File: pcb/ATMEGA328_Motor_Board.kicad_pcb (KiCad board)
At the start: 2 copper layers, 77 x 100 mm, 145 parts, among them P1 CONN_01X04, P10 CONN_01X04, P11 CONN_01X02, P12 CONN_01X03, P13 CONN_01X02, P14 USB_MINI, P15 CONN_01X02, P16 CONN_02X03, P2 CONN_01X04, P3 CONN_01X03, P4 CONN_01X03, P5 CONN_01X03, P6 CONN_01X03, P7 CONN_01X03, P8 CONN_01X03, P9 CONN_01X04, SW1 Pulsador_4p, U1 ATMEGA328, U2 PCA9685, U3 FT231X, U4 L298P, U5 L298P, U6 TSR_1, U7 LM2903, U8 LM2903

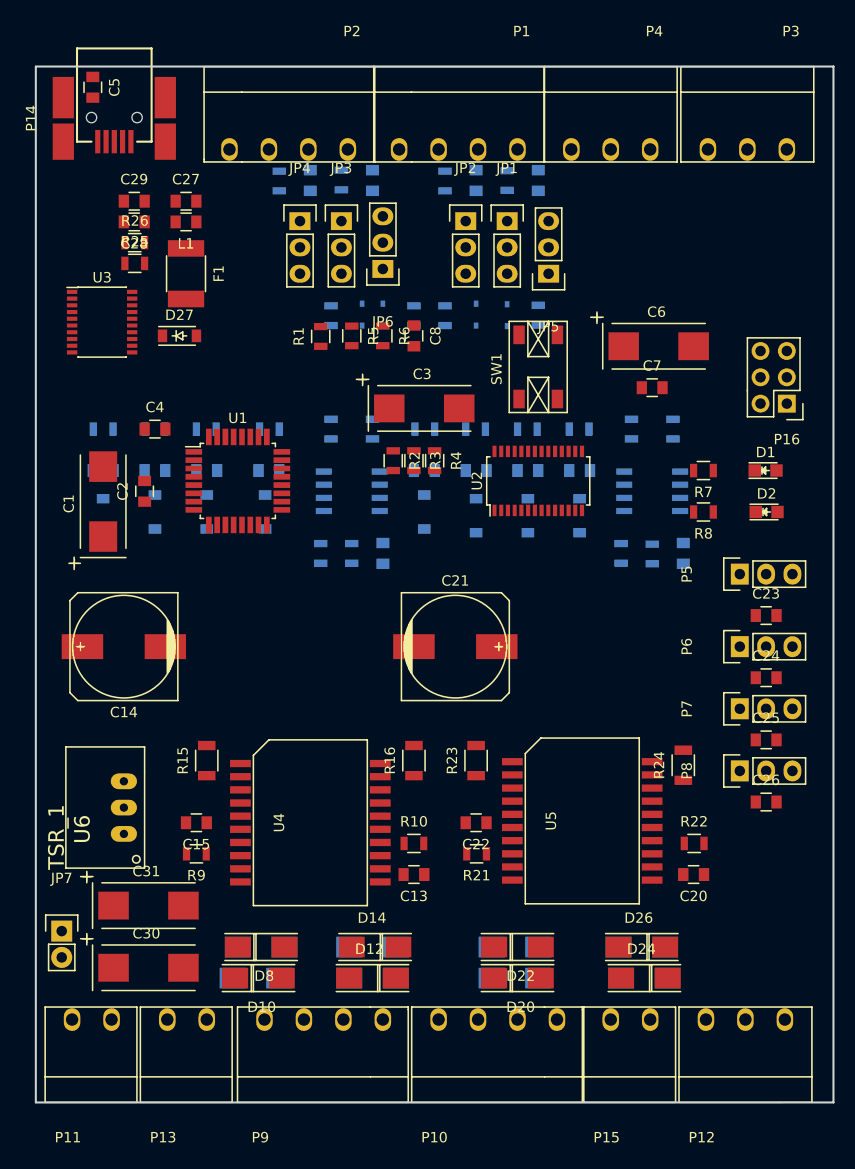
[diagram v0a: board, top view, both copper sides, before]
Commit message: añadida huella para choke alimentacion
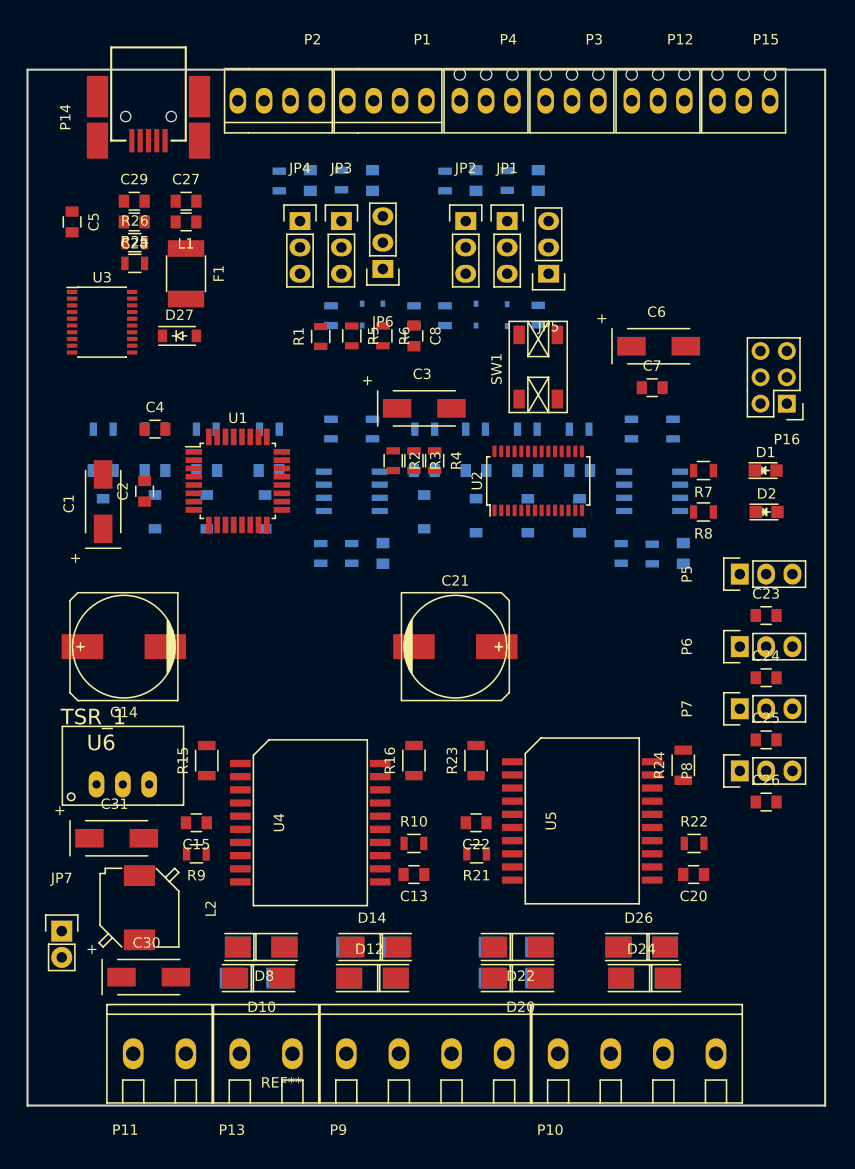
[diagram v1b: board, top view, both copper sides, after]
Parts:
- added L2: 10u, Magneticos:FERROCORE_SMD_0703, F.Cu at (118.5, 121.2)
- C1, C3, C30, C31, C6: footprint Condensadores:TantalC_SizeD_EIA-7343_Wave -> Condensadores:TantalC_SizeC_EIA-6032_Wave
- P1, P2: footprint PhoenixContact:PhoenixContact_MC_1_5x4x3_81 -> PhoenixContact:PhoenixContact_MPT_0,5_4-2,54
- P10, P9: footprint PhoenixContact:PhoenixContact_MC_1_5x4x3_81 -> PhoenixContact:PhoenixContact_mkdsn_4_5.08
- P11, P13: footprint PhoenixContact:PhoenixContact_MC_1_5x2x3_81 -> PhoenixContact:PhoenixContact_mkdsn_2_5.08
- P12, P3, P4: footprint PhoenixContact:PhoenixContact_MC_1_5x3x3_81 -> PhoenixContact:PhoenixContact_MPT_0,5_3-2,54
- P15: footprint PhoenixContact:PhoenixContact_MC_1_5x2x3_81 -> PhoenixContact:PhoenixContact_MPT_0,5_3-2,54
- REF**: moved to F.Cu
- moved P15 90.0 mm to (179.4, 43.3), turned to 180 degrees
- moved P12 88.7 mm to (171.1, 43.3), turned to 180 degrees
- moved P3 18.8 mm to (162.8, 43.3)
- moved P4 14.1 mm to (154.5, 43.3)
- moved C5 13.2 mm to (112.0, 55.0)
- moved P10 12.0 mm to (158.9, 135.3)
- moved U6 10.0 mm to (111.1, 111.3), turned to 0 degrees
- moved P1 9.98 mm to (146.2, 43.3)
- moved P9 8.56 mm to (138.5, 135.3)
- moved P13 7.74 mm to (128.2, 135.3)
- moved C31 7.19 mm to (116.3, 114.5)
- moved P11 6.76 mm to (117.9, 135.3)
- moved P2 5.58 mm to (135.6, 43.3)
- moved P14 3.30 mm to (119.4, 47.1)
- moved C30 0.90 mm to (119.4, 127.9)
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
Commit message: se añaden optos para E/S y cristal
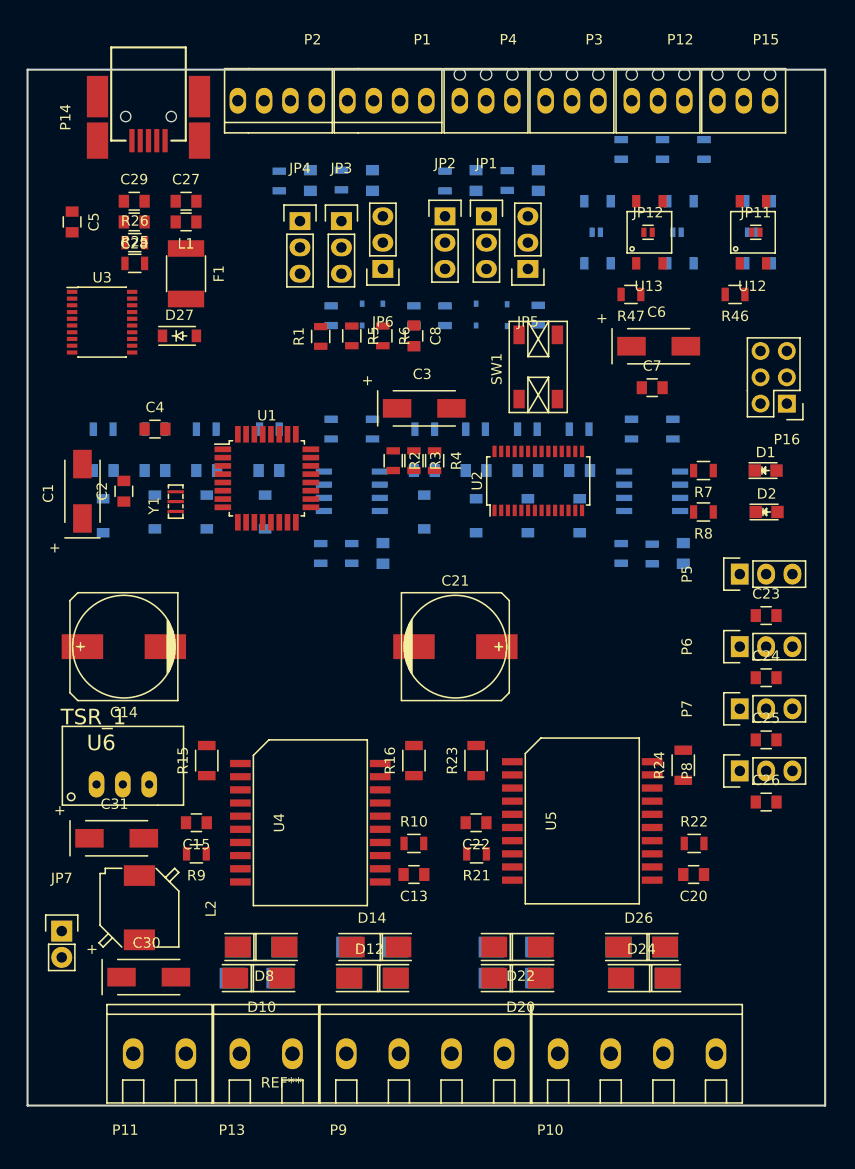
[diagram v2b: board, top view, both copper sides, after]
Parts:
- added JP10: Jumper_NO_Small, Vias:JMP_0603, B.Cu at (177.6, 56.0)
- added JP11: Jumper_NO_Small, Vias:JMP_0603, F.Cu at (178.0, 56.0)
- added JP12: Jumper_NO_Small, Vias:JMP_0603, F.Cu at (167.6, 56.0)
- added JP8: Jumper_NO_Small, Vias:JMP_0603, B.Cu at (162.6, 56.0)
- added JP9: Jumper_NO_Small, Vias:JMP_0603, B.Cu at (170.4, 56.0)
- added R43: R, Resistors_SMD:R_0805, B.Cu at (165.0, 48.0)
- added R44: R, Resistors_SMD:R_0805, B.Cu at (169.0, 48.0)
- added R45: R, Resistors_SMD:R_0805, B.Cu at (173.0, 48.0)
- added R46: R, Resistors_SMD:R_0805, F.Cu at (176.0, 62.0)
- added R47: R, Resistors_SMD:R_0805, F.Cu at (165.9, 62.0)
- added U10: VOM617A, SOP:SOP-4, B.Cu at (172.0, 59.0)
- added U11: VOM617A, SOP:SOP-4, B.Cu at (179.5, 59.0)
- added U12: ASSR-1218, SOP:SOP-4, F.Cu at (176.5, 59.0)
- added U13: ASSR-1218, SOP:SOP-4, F.Cu at (166.5, 59.0)
- added U9: VOM617A, SOP:SOP-4, B.Cu at (164.0, 59.0)
- added Y1: 16MHz, Cristal:Murata_CSTCE_V_A, F.Cu at (122.0, 82.0)
- moved U1 2.81 mm to (130.8, 79.8)
- moved C1 2.24 mm to (113.0, 81.0)
- moved JP1 2.05 mm to (152.0, 54.5)
- moved JP2 2.05 mm to (148.0, 54.5)
- moved JP5 2.05 mm to (156.0, 59.5)
- moved C2 2.00 mm to (117.0, 81.0)
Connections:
- U1 pad 10: DI1 -> uC_DI1
- U1 pad 11: DI2 -> uC_DI2
- U1 pad 12: DI3 -> uC_DI3
- U1 pad 13: DO1 -> uC_DO1
- U1 pad 14: DO2 -> uC_DO2

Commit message: comienzo a ordenar paquetes y rutado de potencia
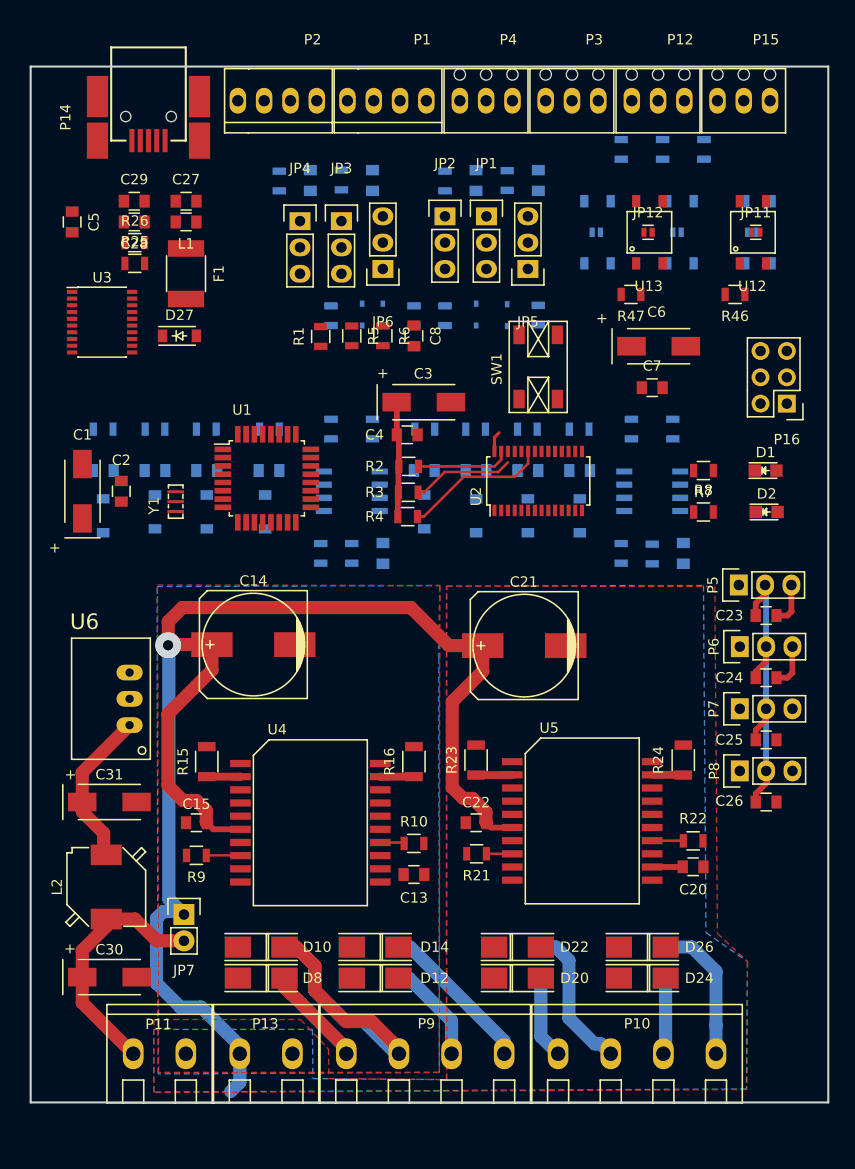
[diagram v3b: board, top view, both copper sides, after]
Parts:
- moved C4 24.4 mm to (144.3, 75.5)
- moved C14 12.5 mm to (129.5, 95.8)
- moved JP7 11.9 mm to (122.8, 121.9)
- moved U6 9.57 mm to (119.5, 106.9), turned to 90 degrees
- moved C21 6.65 mm to (155.7, 95.9), turned to 180 degrees
- moved R4 5.99 mm to (144.4, 83.5), turned to 0 degrees
- moved C30 3.80 mm to (115.6, 127.9)
- moved L2 3.77 mm to (115.3, 119.2)
- moved C31 3.57 mm to (115.6, 111.0)
- moved R3 3.10 mm to (144.4, 81.1), turned to 0 degrees
- moved D10 3.01 mm to (130.2, 125.0), turned to 180 degrees
- moved D11 3.01 mm to (141.2, 128.0), turned to 0 degrees
- moved D13 3.01 mm to (141.2, 125.0), turned to 0 degrees
- moved D19 3.01 mm to (155.0, 128.0)
- moved D21 3.01 mm to (155.0, 125.0)
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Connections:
- C30 pad 1: VSS -> +24V
- L2 pad 1: VSS -> +24V
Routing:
- net VSS: track 0.00 -> 137.9 mm, vias 0 -> 1
- net +5V: track 0.00 -> 47.2 mm
- net Motor1-: track 0.00 -> 33.7 mm
- net +24V: track 0.00 -> 24.4 mm
- net Motor1+: track 0.00 -> 19.6 mm
- net Net-(C31-Pad1): track 0.00 -> 15.4 mm
- net Motor2-: track 0.00 -> 15.2 mm
- net Motor3-: track 0.00 -> 14.3 mm
- net /Control/PWM_OE: track 0.00 -> 14.0 mm
- net Motor4-: track 0.00 -> 13.8 mm
- net Motor2+: track 0.00 -> 10.0 mm
- net /Control/SCL: track 0.00 -> 9.87 mm
- net /Control/SDA: track 0.00 -> 9.05 mm
- net GND: track 0.00 -> 8.43 mm
- net Motor3+: track 0.00 -> 7.99 mm
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- added copper zone on B.Cu, net GND
- added copper zone on F.Cu, net GND
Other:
- net class Default: clearance 0.2 -> 0.2032; trace_width 0.25 -> 0.254
- net class Potencia added: clearance 0.4064, trace_width 1.27, via_dia 4, via_drill 1
- rule trace_clearance: 0.2 -> 0.2032

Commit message: finalizado el posicionado sobre la pcb
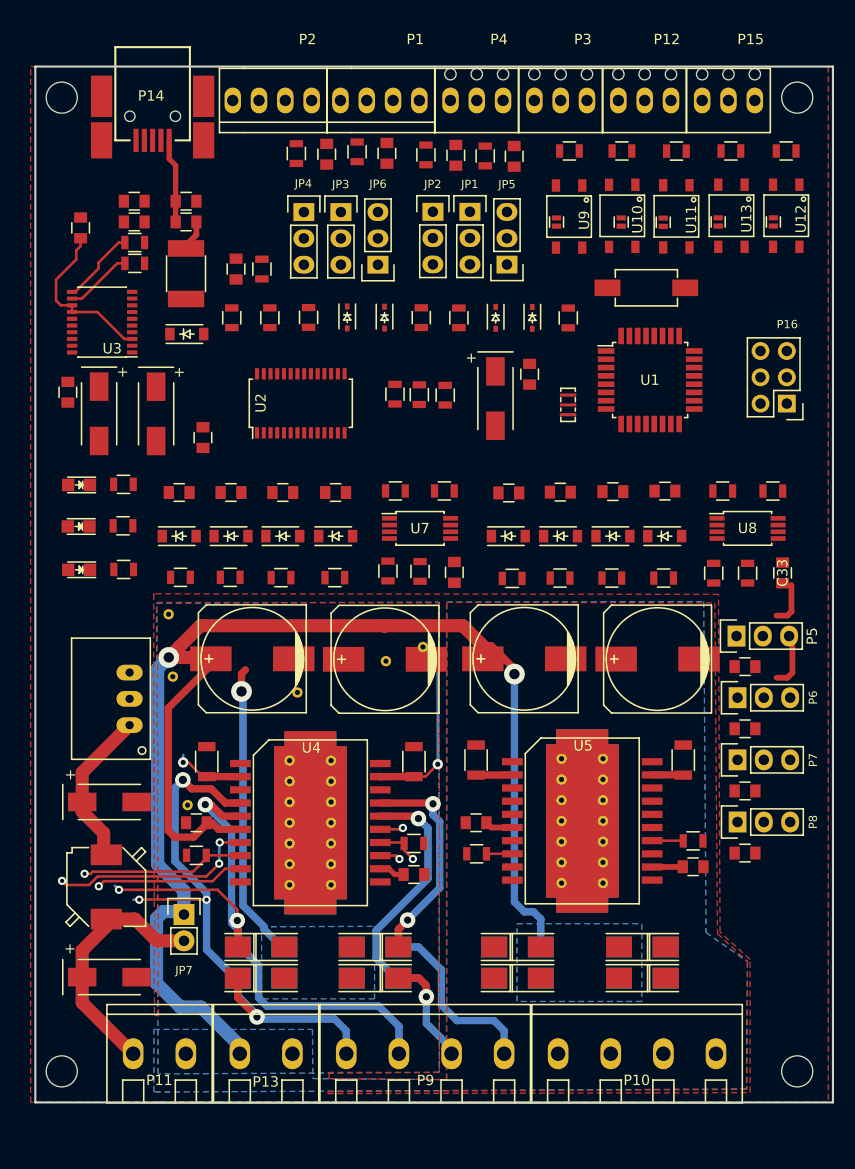
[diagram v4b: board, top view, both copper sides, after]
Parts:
- added C38: 220u, Capacitors_SMD:c_elec_10x10, F.Cu at (142.2, 97.2)
- added C39: 220u, Capacitors_SMD:c_elec_10x10, F.Cu at (168.5, 97.2)
- added D32: LED, Leds:LED_0805, F.Cu at (112.7, 88.6)
- added Gnd-Via: VAL**, Vias:Gnd-Via, F.Cu at (182.0, 137.0)
- added Gnd-Via: VAL**, Vias:Gnd-Via, F.Cu at (145.9, 96.0)
- added Gnd-Via: VAL**, Vias:Gnd-Via, F.Cu at (182.0, 43.0)
- added Gnd-Via: VAL**, Vias:Gnd-Via, F.Cu at (111.0, 43.0)
- added Gnd-Via: VAL**, Vias:Gnd-Via, F.Cu at (111.0, 137.0)
- added Gnd-Via: VAL**, Vias:Gnd-Via, F.Cu at (121.3, 92.9)
- added Gnd-Via: VAL**, Vias:Gnd-Via, F.Cu at (121.7, 98.9)
- added Gnd-Via: VAL**, Vias:Gnd-Via, F.Cu at (123.2, 111.3)
- added Gnd-Via: VAL**, Vias:Gnd-Via, F.Cu at (133.8, 100.4)
- added Gnd-Via: VAL**, Vias:Gnd-Via, F.Cu at (142.3, 97.4)
- added R48: R, Resistors_SMD:R_0805, F.Cu at (117.0, 88.5)
- C10, C11, C12, C16, C17, C18, C19, C32, C33, C34, C35, C36, C37, C9, D15, D16, D17, D18, D28, D29, D3, D30, D31, D4, D5, D6, JP10, JP8, JP9, R11, R12, R13, R14, R17, R18, R19, R20, R27, R28, R29, R30, R31, R32, R33, R34, R35, R36, R37, R38, R39, R40, R41, R42, R43, R44, R45, U10, U11, U9: moved to F.Cu
- SW1: value Pulsador_4p -> Pulsador_2p; footprint Relays_and_Contacts:ALP_SKQGAKE010 -> Relays_and_Contacts:CANAL_ELECTRONIC_DTSM-31N-B
- U7, U8: footprint Housings_SOIC:SOIC-8_3.9x4.9mm_Pitch1.27mm -> Housings_SSOP:TSSOP-8_4.4x3mm_Pitch0.65mm; moved to F.Cu
- moved D1 66.5 mm to (112.6, 84.4), turned to 180 degrees
- moved D2 66.4 mm to (112.7, 80.4), turned to 180 degrees
- moved C7 56.4 mm to (111.6, 71.4), turned to 270 degrees
- moved R7 56.3 mm to (116.9, 84.3), turned to 0 degrees
- moved R8 56.1 mm to (117.0, 80.3), turned to 180 degrees
- moved C6 54.4 mm to (114.6, 73.5), turned to 270 degrees
- moved C2 41.0 mm to (156.2, 69.7), turned to 270 degrees
- moved C1 40.9 mm to (152.9, 72.0), turned to 270 degrees
- moved Y1 39.0 mm to (159.9, 72.7)
- moved U1 38.2 mm to (167.8, 70.3)
- moved C3 25.9 mm to (120.1, 73.5), turned to 270 degrees
- moved U2 24.1 mm to (134.1, 72.5)
- moved C4 19.7 mm to (124.6, 75.8), turned to 270 degrees
- moved C8 18.3 mm to (127.8, 59.5), turned to 90 degrees
- moved R47 16.9 mm to (175.6, 48.1)
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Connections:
- SW1 pad 2: GND -> RESET
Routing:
- net +5V: track 47.2 -> 5.44 mm
- net Motor1+: track 19.6 -> 56.0 mm, vias 0 -> 4
- net VSS: track 137.9 -> 172.1 mm, vias 1 -> 3
- net Motor2+: track 10.0 -> 37.3 mm, vias 0 -> 2
- net Motor2-: track 15.2 -> 41.6 mm, vias 0 -> 2
- net Motor1-: track 33.7 -> 58.5 mm, vias 0 -> 3
- net /Potencia/Motor1_A_in: track 0.00 -> 20.3 mm, vias 0 -> 3
- net Net-(C5-Pad1): track 0.00 -> 16.3 mm
- net /Potencia/Motor1_B_in: track 0.00 -> 14.4 mm, vias 0 -> 1
- net Motor3-: track 14.3 -> 0.00 mm
- net /Control/PWM_OE: track 14.0 -> 0.00 mm
- net Motor4-: track 13.8 -> 0.00 mm
- net MOTOR2_SENSE: track 3.25 -> 16.0 mm, vias 0 -> 1
- net MOTOR1_EN: track 3.31 -> 16.0 mm, vias 0 -> 1
- net /Control/SCL: track 9.87 -> 0.00 mm
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- added copper zone on B.Cu, net VSS
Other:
- net class Potencia: clearance 0.4064 -> 0.3048; trace_width 1.27 -> 0.7112; via_dia 4 -> 1.5; via_drill 1 -> 0.7

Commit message: planos en ambas caras, restan 63 nodos
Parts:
- removed the Gnd-Via at (121.3, 92.9)
- added Gnd-Via: VAL**, Vias:Gnd-Via, F.Cu at (175.6, 115.9)
- added Gnd-Via: VAL**, Vias:Gnd-Via, F.Cu at (161.4, 72.7)
- added Gnd-Via: VAL**, Vias:Gnd-Via, F.Cu at (175.6, 109.9)
- added Gnd-Via: VAL**, Vias:Gnd-Via, F.Cu at (175.6, 103.9)
- added Gnd-Via: VAL**, Vias:Gnd-Via, F.Cu at (175.6, 98.0)
- added Gnd-Via: VAL**, Vias:Gnd-Via, F.Cu at (154.8, 98.3)
- added Gnd-Via: VAL**, Vias:Gnd-Via, F.Cu at (154.8, 97.1)
- moved Gnd-Via 8.89 mm to (154.8, 95.8)
- moved Gnd-Via 7.44 mm to (128.1, 95.6)
- moved C29 4.04 mm to (114.0, 53.1), turned to 90 degrees
- moved R26 2.98 mm to (115.2, 57.8), turned to 90 degrees
- moved C5 2.20 mm to (112.8, 57.8)
- moved C28 1.96 mm to (117.7, 53.1), turned to 90 degrees
- moved C25 1.34 mm to (178.3, 109.9), turned to 180 degrees
- moved R25 1.31 mm to (117.7, 57.8), turned to 90 degrees
- moved C24 1.31 mm to (178.3, 103.9), turned to 180 degrees
- moved C26 1.29 mm to (178.2, 115.9), turned to 180 degrees
- moved C23 1.27 mm to (178.2, 97.9), turned to 180 degrees
- moved JP9 1.18 mm to (163.8, 55.0)
- moved C39 0.67 mm to (167.8, 97.1)
- moved C21 0.67 mm to (155.0, 97.1), turned to 0 degrees
- moved P5 0.55 mm to (176.7, 94.9)
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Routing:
- net +5V: track 5.44 -> 301.4 mm, vias 0 -> 4
- net +24V: track 24.4 -> 198.4 mm, vias 0 -> 1
- net ENC2_B2: track 0.00 -> 67.8 mm, vias 0 -> 3
- net VSS: track 172.1 -> 235.5 mm
- net MOTOR1_EN: track 16.0 -> 70.1 mm, vias 1 -> 2
- net CONSIGNA2: track 0.00 -> 48.8 mm, vias 0 -> 1
- net /Potencia/Motor1_A_in: track 20.3 -> 67.5 mm, vias 3 -> 4
- net /Potencia/Motor1_B_in: track 14.4 -> 61.1 mm, vias 1 -> 2
- net uC_DO1: track 0.00 -> 44.9 mm, vias 0 -> 2
- net /Control/SDA: track 0.00 -> 42.6 mm, vias 0 -> 2
- net Net-(R6-Pad2): track 0.00 -> 42.5 mm, vias 0 -> 2
- net CONSIGNA1: track 0.00 -> 42.1 mm, vias 0 -> 1
- net Motor1+: track 56.0 -> 97.7 mm, vias 4 -> 5
- net /Control/SCL: track 0.00 -> 40.7 mm, vias 0 -> 2
- net uC_DO2: track 0.00 -> 40.4 mm, vias 0 -> 2
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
